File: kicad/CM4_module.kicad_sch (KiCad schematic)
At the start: 1 part

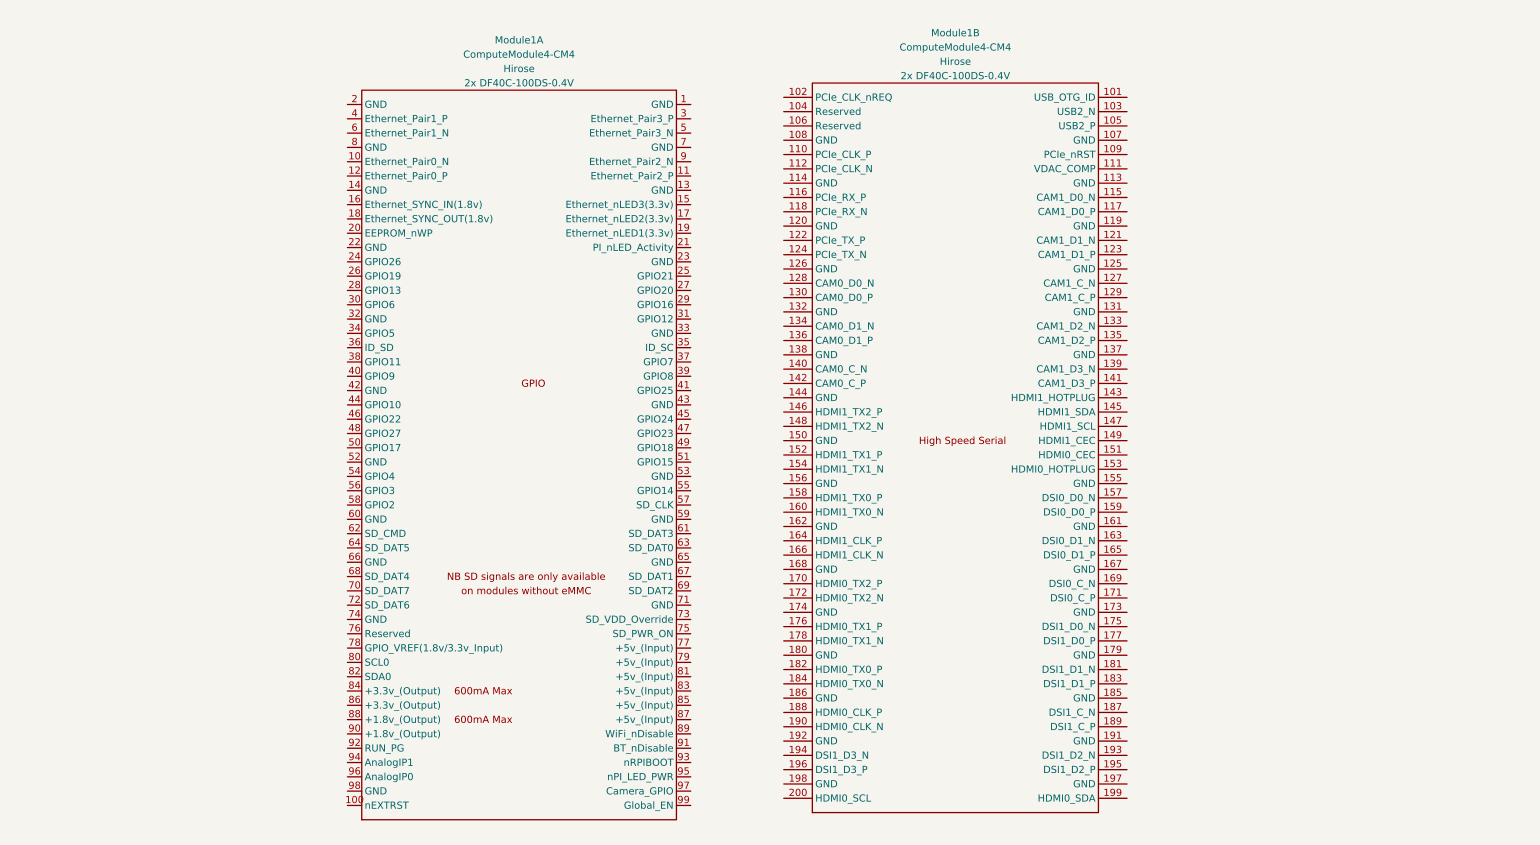
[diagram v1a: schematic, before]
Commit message: Connecting GPIO, GPDI, B2B, SD
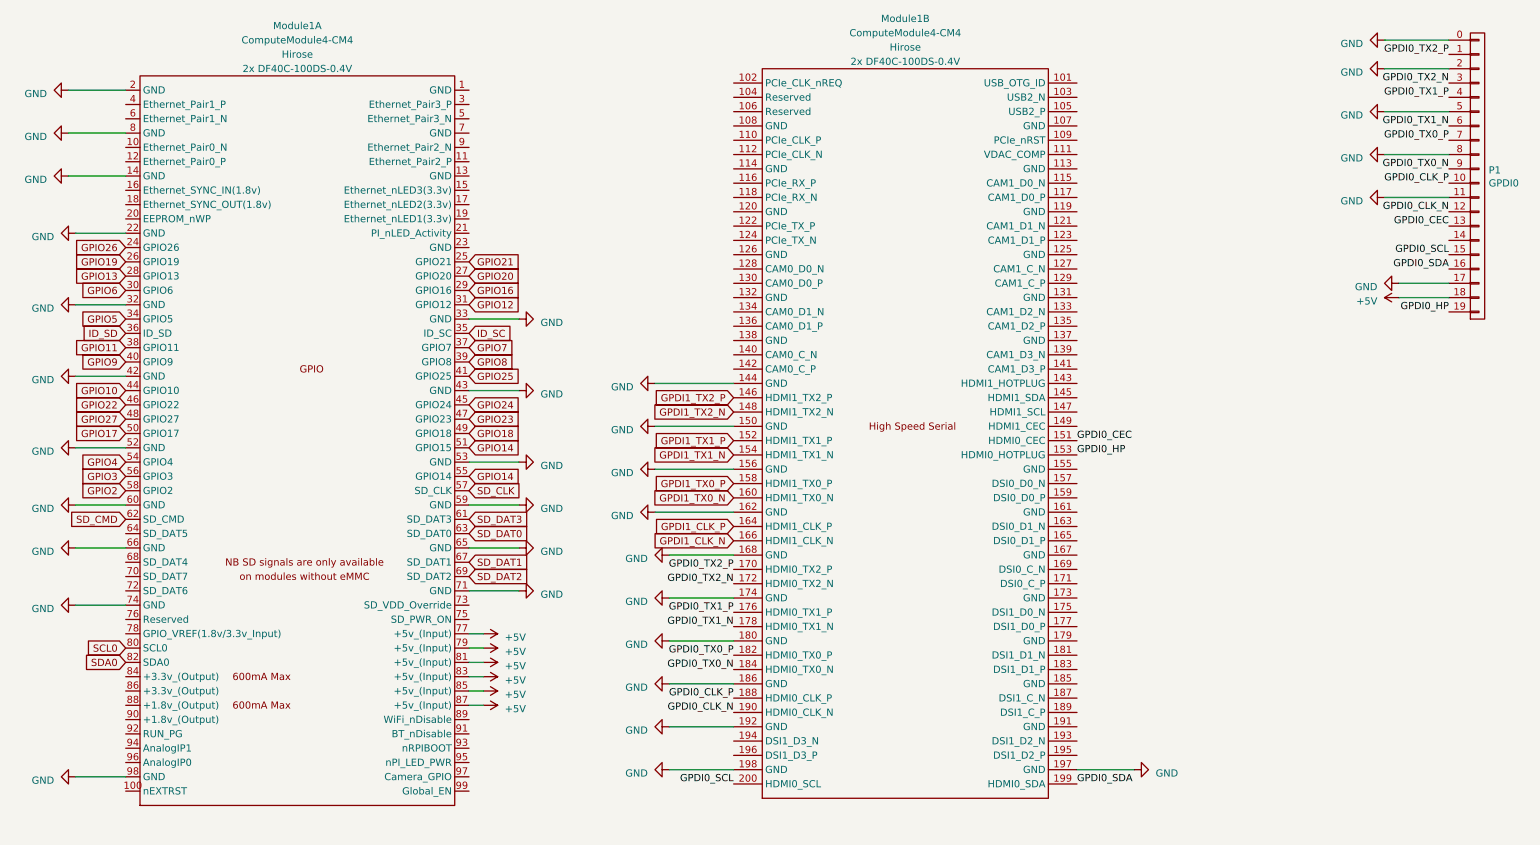
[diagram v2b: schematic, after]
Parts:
- added P1: GPDI0, conn-fci:CONN-10029449-111RLF, symbol hdmi-d:HDMI-D
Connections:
- net GND: now reaches Module1.144 (GND)
- net GND: now also Module1.14 (GND), Module1.150 (GND), Module1.156 (GND), Module1.162 (GND), Module1.168 (GND), Module1.174 (GND), Module1.180 (GND), Module1.186 (GND), Module1.192 (GND), Module1.197 (GND), Module1.198 (GND), Module1.2 (GND), Module1.22 (GND), Module1.32 (GND), Module1.33 (GND), Module1.42 (GND), Module1.43 (GND), Module1.52 (GND), Module1.53 (GND), Module1.59 (GND), Module1.60 (GND), Module1.65 (GND), Module1.66 (GND), Module1.71 (GND), Module1.74 (GND), Module1.8 (GND), Module1.98 (GND), P1.0, P1.11 (P11), P1.17 (P17), P1.2 (P2), P1.5 (P5), P1.8 (P8)
- net GPDI1_TX2_P: now reaches Module1.146 (HDMI1_TX2_P)
- net GPDI1_TX2_N: now reaches Module1.148 (HDMI1_TX2_N)
- net GPDI0_CEC: now reaches Module1.151 (HDMI0_CEC)
- net GPDI0_CEC: now also P1.13 (P13)
- net GPDI1_TX1_P: now reaches Module1.152 (HDMI1_TX1_P)
- net GPDI0_HP: now reaches Module1.153 (HDMI0_HOTPLUG)
- net GPDI0_HP: now also P1.19 (P19)
- net GPDI1_TX1_N: now reaches Module1.154 (HDMI1_TX1_N)
- net GPDI1_TX0_P: now reaches Module1.158 (HDMI1_TX0_P)
- net GPDI1_TX0_N: now reaches Module1.160 (HDMI1_TX0_N)
- net GPDI1_CLK_P: now reaches Module1.164 (HDMI1_CLK_P)
- net GPDI1_CLK_N: now reaches Module1.166 (HDMI1_CLK_N)
- net GPDI0_TX2_P: now reaches Module1.170 (HDMI0_TX2_P)
- net GPDI0_TX2_P: now also P1.1 (P1)
- net GPDI0_TX2_N: now reaches Module1.172 (HDMI0_TX2_N)
- net GPDI0_TX2_N: now also P1.3 (P3)
- net GPDI0_TX1_P: now reaches Module1.176 (HDMI0_TX1_P)
- net GPDI0_TX1_P: now also P1.4 (P4)
- net GPDI0_TX1_N: now reaches Module1.178 (HDMI0_TX1_N)
- net GPDI0_TX1_N: now also P1.6 (P6)
- net GPDI0_TX0_P: now reaches Module1.182 (HDMI0_TX0_P)
- net GPDI0_TX0_P: now also P1.7 (P7)
- net GPDI0_TX0_N: now reaches Module1.184 (HDMI0_TX0_N)
- net GPDI0_TX0_N: now also P1.9 (P9)
- net GPDI0_CLK_P: now reaches Module1.188 (HDMI0_CLK_P)
- net GPDI0_CLK_P: now also P1.10 (P10)
- net GPDI0_CLK_N: now reaches Module1.190 (HDMI0_CLK_N)
- net GPDI0_CLK_N: now also P1.12 (P12)
- net GPDI0_SDA: now reaches Module1.199 (HDMI0_SDA)
- net GPDI0_SDA: now also P1.16 (P16)
- net GPDI0_SCL: now reaches Module1.200 (HDMI0_SCL)
- net GPDI0_SCL: now also P1.15 (P15)
- net GPIO26: now reaches Module1.24 (GPIO26)
- net GPIO21: now reaches Module1.25 (GPIO21)
- net GPIO19: now reaches Module1.26 (GPIO19)
- net GPIO20: now reaches Module1.27 (GPIO20)
- net GPIO13: now reaches Module1.28 (GPIO13)
- net GPIO16: now reaches Module1.29 (GPIO16)
- net GPIO6: now reaches Module1.30 (GPIO6)
- net GPIO12: now reaches Module1.31 (GPIO12)
- net GPIO5: now reaches Module1.34 (GPIO5)
- net ID_SC: now reaches Module1.35 (ID_SC)
- net ID_SD: now reaches Module1.36 (ID_SD)
- net GPIO7: now reaches Module1.37 (GPIO7)
- net GPIO11: now reaches Module1.38 (GPIO11)
- net GPIO8: now reaches Module1.39 (GPIO8)
- net GPIO9: now reaches Module1.40 (GPIO9)
- net GPIO25: now reaches Module1.41 (GPIO25)
- net GPIO10: now reaches Module1.44 (GPIO10)
- net GPIO24: now reaches Module1.45 (GPIO24)
- net GPIO22: now reaches Module1.46 (GPIO22)
- net GPIO23: now reaches Module1.47 (GPIO23)
- net GPIO27: now reaches Module1.48 (GPIO27)
- net GPIO18: now reaches Module1.49 (GPIO18)
- net GPIO17: now reaches Module1.50 (GPIO17)
- net GPIO14: now reaches Module1.51 (GPIO15)
- net GPIO14: now also Module1.55 (GPIO14)
- net GPIO4: now reaches Module1.54 (GPIO4)
- net GPIO3: now reaches Module1.56 (GPIO3)
- net SD_CLK: now reaches Module1.57 (SD_CLK)
- net GPIO2: now reaches Module1.58 (GPIO2)
- net SD_DAT3: now reaches Module1.61 (SD_DAT3)
- net SD_CMD: now reaches Module1.62 (SD_CMD)
- net SD_DAT0: now reaches Module1.63 (SD_DAT0)
- net SD_DAT1: now reaches Module1.67 (SD_DAT1)
- net SD_DAT2: now reaches Module1.69 (SD_DAT2)
- net +5V: now reaches Module1.77 (+5v_(Input))
- net +5V: now also Module1.79 (+5v_(Input)), Module1.81 (+5v_(Input)), Module1.83 (+5v_(Input)), Module1.85 (+5v_(Input)), Module1.87 (+5v_(Input)), P1.18 (P18)
- net SCL0: now reaches Module1.80 (SCL0)
- net SDA0: now reaches Module1.82 (SDA0)
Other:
- moved on the sheet: Module1A, Module1B

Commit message: finalising connections
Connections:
- net GND: now also Module1.1 (GND), Module1.107 (GND), Module1.108 (GND), Module1.113 (GND), Module1.114 (GND), Module1.119 (GND), Module1.120 (GND), Module1.125 (GND), Module1.126 (GND), Module1.13 (GND), Module1.131 (GND), Module1.132 (GND), Module1.137 (GND), Module1.138 (GND), Module1.155 (GND), Module1.161 (GND), Module1.167 (GND), Module1.173 (GND), Module1.179 (GND), Module1.185 (GND), Module1.191 (GND), Module1.23 (GND), Module1.7 (GND)
- net USB_OTG_ID: now reaches Module1.101 (USB_OTG_ID)
- net PCIe_CLK_nREQ: now reaches Module1.102 (PCIe_CLK_nREQ)
- net USB2_N: now reaches Module1.103 (USB2_N)
- net USB2_P: now reaches Module1.105 (USB2_P)
- net PCIe_nRST: now reaches Module1.109 (PCIe_nRST)
- net PCIe_CLK_P: now reaches Module1.110 (PCIe_CLK_P)
- net PCIe_CLK_N: now reaches Module1.112 (PCIe_CLK_N)
- net CAM1_D0_N: now reaches Module1.115 (CAM1_D0_N)
- net PCIe_RX_P: now reaches Module1.116 (PCIe_RX_P)
- net CAM1_D0_P: now reaches Module1.117 (CAM1_D0_P)
- net PCIe_RX_N: now reaches Module1.118 (PCIe_RX_N)
- net CAM1_D1_N: now reaches Module1.121 (CAM1_D1_N)
- net PCIe_TX_P: now reaches Module1.122 (PCIe_TX_P)
- net CAM1_D1_P: now reaches Module1.123 (CAM1_D1_P)
- net PCIe_TX_N: now reaches Module1.124 (PCIe_TX_N)
- net CAM1_C_N: now reaches Module1.127 (CAM1_C_N)
- net CAM0_D0_N: now reaches Module1.128 (CAM0_D0_N)
- net CAM1_C_P: now reaches Module1.129 (CAM1_C_P)
- net CAM0_D0_P: now reaches Module1.130 (CAM0_D0_P)
- net CAM0_D1_N: now reaches Module1.134 (CAM0_D1_N)
- net CAM0_D1_P: now reaches Module1.136 (CAM0_D1_P)
- net CAM0_C_P: now reaches Module1.140 (CAM0_C_N)
- net CAM0_C_N: now reaches Module1.142 (CAM0_C_P)
- net GPDI1_HP_PD: now reaches Module1.143 (HDMI1_HOTPLUG)
- net GPDI1_SDA_5VPU: now reaches Module1.145 (HDMI1_SDA)
- net GPDI1_SCL_5VPU: now reaches Module1.147 (HDMI1_SCL)
- net GPDI1_CEC_PU: now reaches Module1.149 (HDMI1_CEC)
- net DSI0_D0_N: now reaches Module1.157 (DSI0_D0_N)
- net DSI0_D0_P: now reaches Module1.159 (DSI0_D0_P)
- net DSI0_D1_N: now reaches Module1.163 (DSI0_D1_N)
- net DSI0_D1_P: now reaches Module1.165 (DSI0_D1_P)
- net DSI0_C_N: now reaches Module1.169 (DSI0_C_N)
- net DSI0_C_P: now reaches Module1.171 (DSI0_C_P)
- net DSI1_D0_S5_N: now reaches Module1.175 (DSI1_D0_N)
- net DSI1_D0_S5_P: now reaches Module1.177 (DSI1_D0_P)
- net DSI1_D1_S7_N: now reaches Module1.181 (DSI1_D1_N)
- net DSI1_D1_S7_P: now reaches Module1.183 (DSI1_D1_P)
- net DSI1_C_S1_N: now reaches Module1.187 (DSI1_C_N)
- net DSI1_C_S1_P: now reaches Module1.189 (DSI1_C_P)
- net DSI1_D2_N: now reaches Module1.193 (DSI1_D2_N)
- net DSI1_D3_N: now reaches Module1.194 (DSI1_D3_N)
- net DSI1_D2_P: now reaches Module1.195 (DSI1_D2_P)
- net DSI1_D3_P: now reaches Module1.196 (DSI1_D3_P)
- net ETH0_N: now reaches Module1.10 (Ethernet_Pair0_N)
- net ETH2_P: now reaches Module1.11 (Ethernet_Pair2_P)
- net ETH0_P: now reaches Module1.12 (Ethernet_Pair0_P)
- net ETH3_P: now reaches Module1.3 (Ethernet_Pair3_P)
- net ETH1_P: now reaches Module1.4 (Ethernet_Pair1_P)
- net ETH3_N: now reaches Module1.5 (Ethernet_Pair3_N)
- net ETH1_N: now reaches Module1.6 (Ethernet_Pair1_N)
- net SD_PWR_ON: now reaches Module1.75 (SD_PWR_ON)
- net +3.3V: now reaches Module1.84 (+3.3v_(Output))
- net +3.3V: now also Module1.86 (+3.3v_(Output))
- net ETH2_N: now reaches Module1.9 (Ethernet_Pair2_N)
- net Camera_GPIO: now reaches Module1.97 (Camera_GPIO)
- no-connect marks 0 -> 33

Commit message: uređena schema
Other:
- company: (none) -> ${project_creator} 
- title: (none) -> ${project_name}  ${project_version}
- moved on the sheet: P1
